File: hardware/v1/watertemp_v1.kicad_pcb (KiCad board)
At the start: 2 copper layers, 37.3 x 93.2 mm, 4 parts, among them P1 Lora, P2 Sensor, P3 Charger

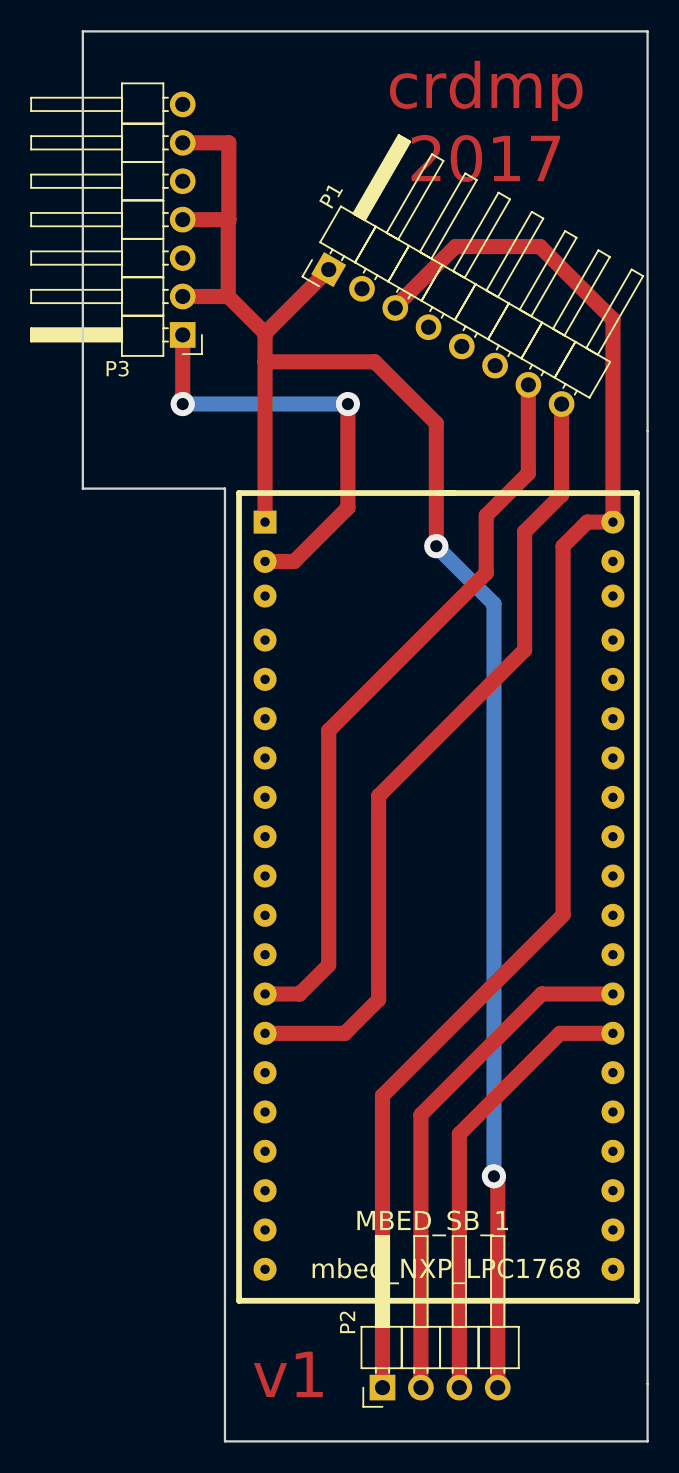
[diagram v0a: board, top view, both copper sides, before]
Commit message: Unified drill hole sizes
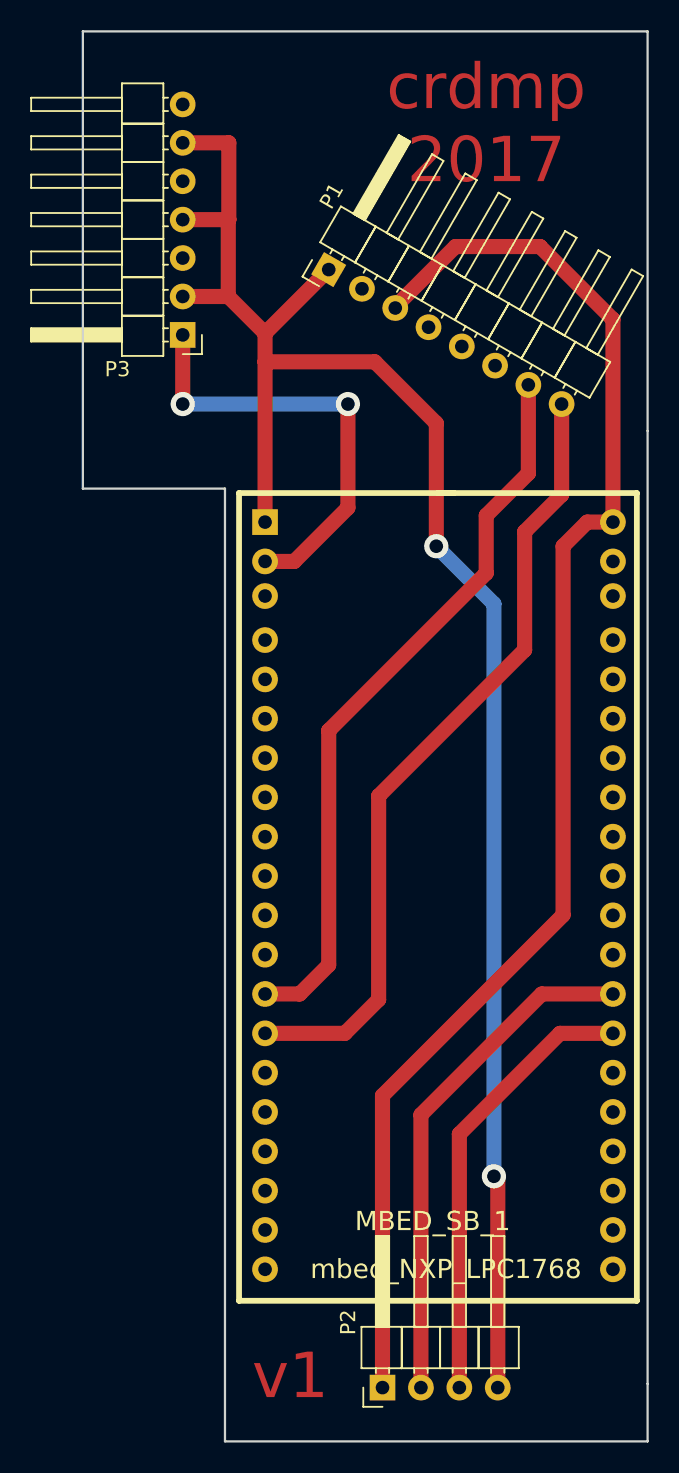
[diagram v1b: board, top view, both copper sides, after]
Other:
- net class Default: via_drill 0.8 -> 0.9
